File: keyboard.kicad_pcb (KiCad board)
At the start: 2 copper layers, 208.8 x 114.3 mm, 52 parts, among them J1 TRRS, SW00 Key, SW01 Key, SW02 Key, SW03 Key, SW04 Key, SW05 Key, SW10 Key, SW11 Key, SW12 Key, SW13 Key, SW14 Key, SW15 Key, SW16 Key, SW17 Key, SW18 Key, SW20 Key, SW21 Key, SW22 Key, SW23 Key, SW24 Key, SW25 Key, SW26 Key, SW27 Key, SW28 Key, SW30 Key, SW31 Key, SW32 Key, SW33 Key, SW34 Key, SW35 Key, SW36 Key, SW37 Key, SW38 Key, SW40 Key, SW41 Key, SW42 Key, SW43 Key, SW44 Key, SW45 Key, SW46 Key, SW47 Key, SW48 Key, U1 ProMicro

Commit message: rename files
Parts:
- H1: footprint myles-keyboard:RightPlate -> keyboard:RightPlate
- J1: footprint myles-keyboard:PJ-320A -> keyboard:PJ-320A
- JP1, JP2: footprint myles-keyboard:Jumper -> keyboard:Jumper
- JP3, JP4: footprint myles-keyboard:JumperSplit -> keyboard:JumperSplit
- R1, R2: footprint myles-keyboard:SDR18 -> keyboard:SDR18
- SW00, SW04, SW05, SW10, SW14, SW20, SW30: footprint myles-keyboard:KeyLeft -> keyboard:KeyLeft
- SW01, SW02, SW11, SW12, SW13, SW15, SW16, SW17, SW21, SW22, SW23, SW24, SW25, SW26, SW27, SW31, SW32, SW33, SW34, SW35, SW36, SW37, SW40, SW41, SW42, SW43, SW44, SW46, SW47: footprint myles-keyboard:Key -> keyboard:Key
- SW03, SW18, SW28, SW38, SW45, SW48: footprint myles-keyboard:KeyRight -> keyboard:KeyRight
- SW_RST1: footprint myles-keyboard:PTS636 -> keyboard:PTS636
- U1: footprint myles-keyboard:ProMicro -> keyboard:ProMicro

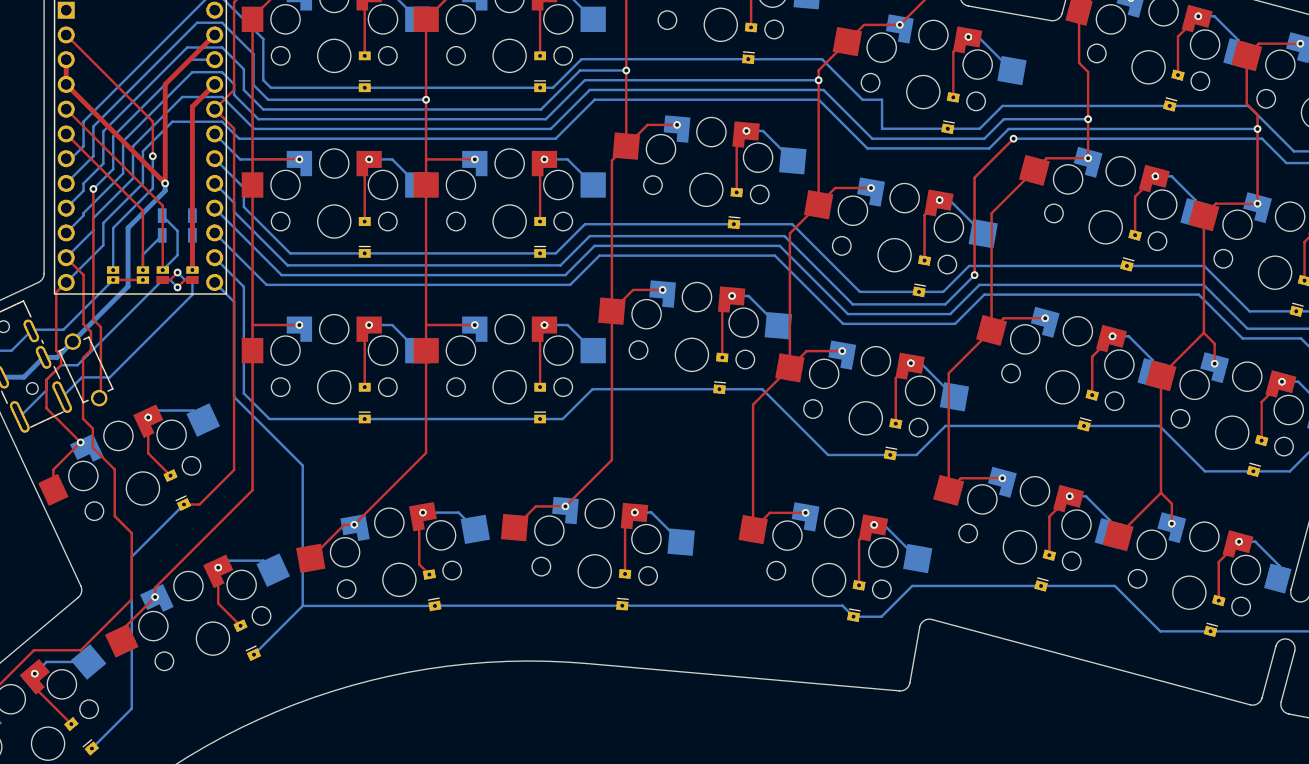
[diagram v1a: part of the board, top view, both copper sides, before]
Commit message: adjust plates and pcb; remove reset button
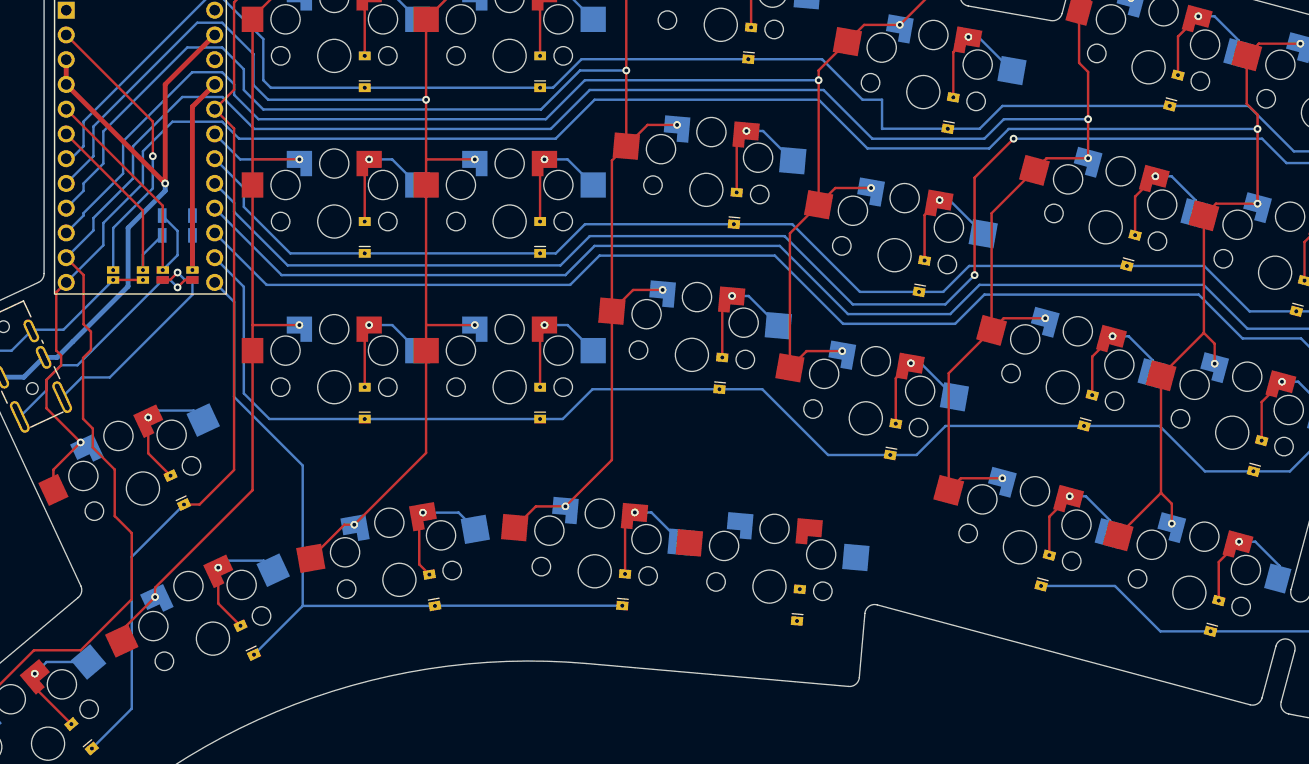
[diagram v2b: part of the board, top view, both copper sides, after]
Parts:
- removed SW_RST1: SW_Push, keyboard:PTS636
- moved SW43 6.16 mm to (124.4, 114.0), turned to -5 degrees
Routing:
- net row4: track 203.9 -> 159.1 mm
- net RESET: track 41.8 -> 0.00 mm, vias 1 -> 0
- net col3: track 201.4 -> 175.5 mm, vias 6 -> 5
- net Net-(SW43-Pad3): track 12.7 -> 0.00 mm, vias 1 -> 0
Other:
- outline, holes or cut-outs redrawn

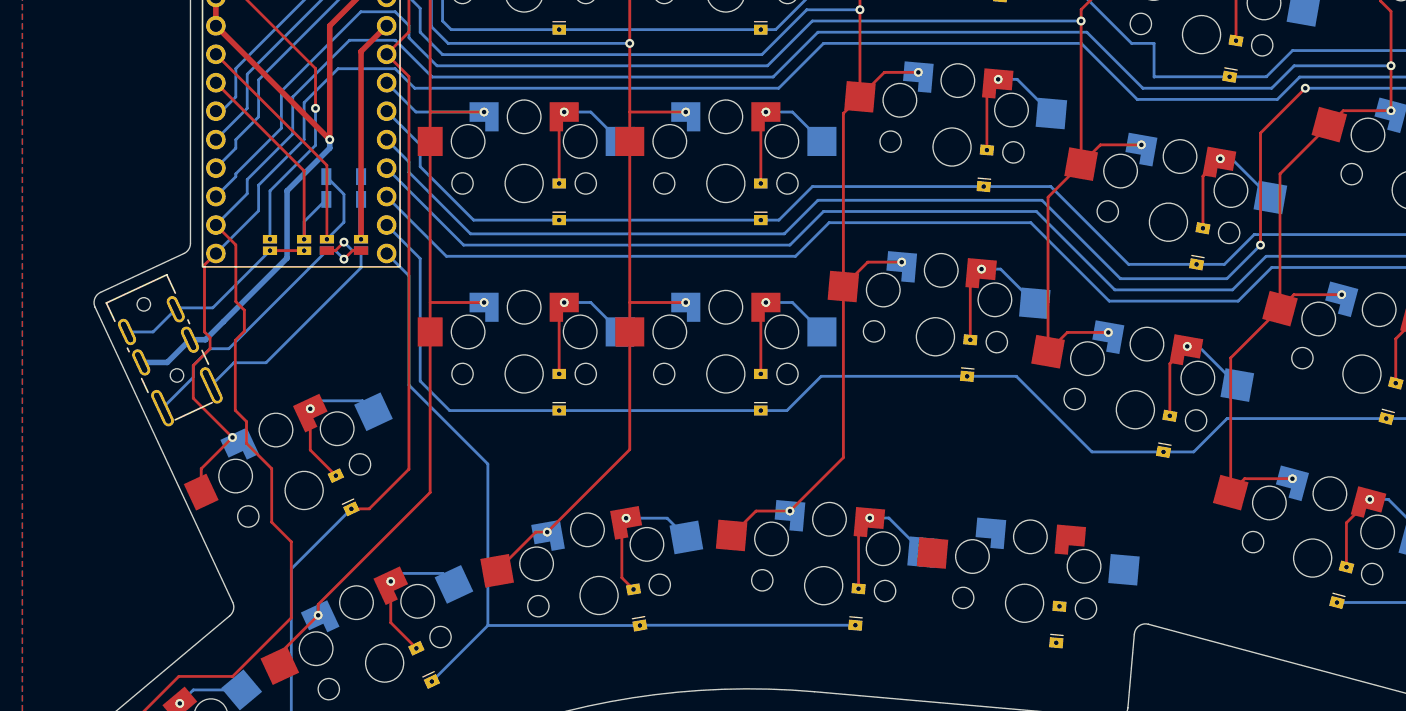
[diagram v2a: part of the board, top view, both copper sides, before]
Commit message: add symbol and footprint for new thin reset button
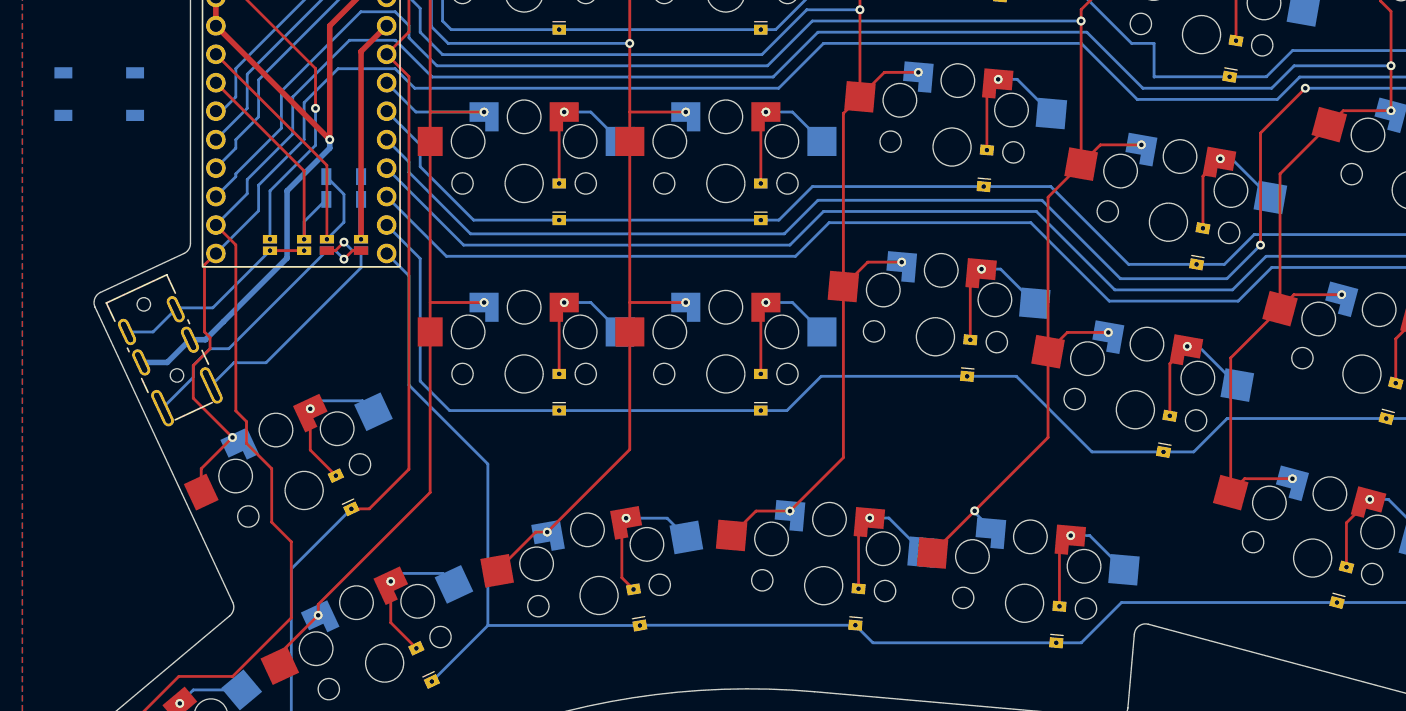
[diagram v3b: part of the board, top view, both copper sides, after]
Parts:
- added SW_RST1: PTS525, keyboard:PTS525, B.Cu at (41.9, 68.5)
- JP1, JP2: value JumperSplit -> Jumper
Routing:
- net row4: track 159.1 -> 204.3 mm
- net col3: track 175.5 -> 199.9 mm, vias 5 -> 6
- net Net-(SW43-Pad3): track 0.00 -> 12.7 mm, vias 0 -> 1
- net col4: track 263.7 -> 263.1 mm

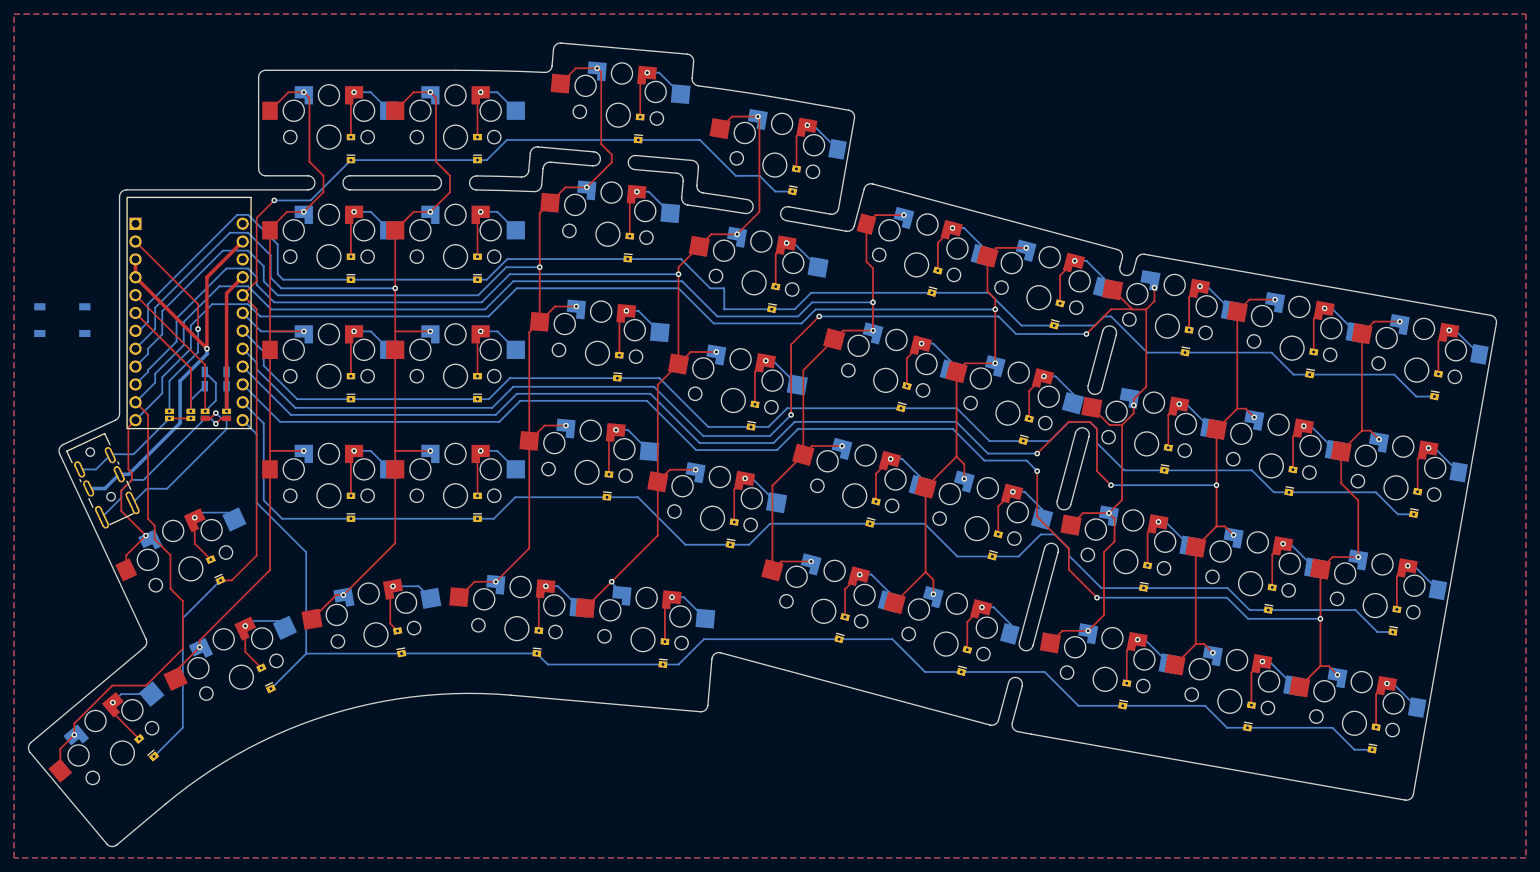
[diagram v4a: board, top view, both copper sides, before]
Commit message: reroute with new layout; use less vias in each switch
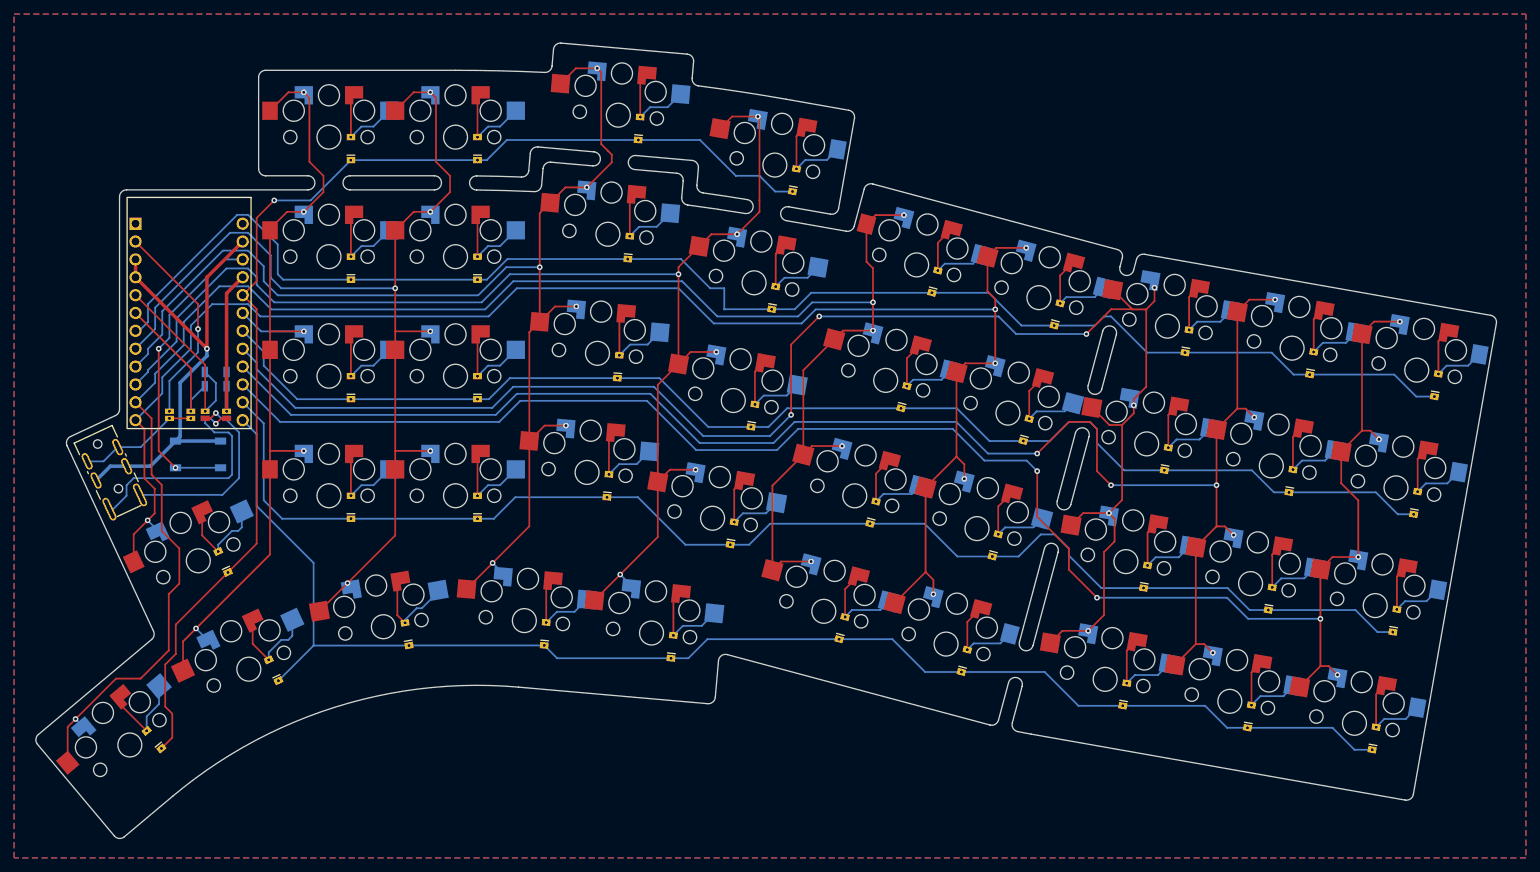
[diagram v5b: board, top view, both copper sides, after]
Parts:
- moved SW_RST1 27.2 mm to (61.2, 87.6), turned to 0 degrees
- moved SW42 1.56 mm to (107.6, 111.3)
- moved SW40 1.56 mm to (68.4, 118.2)
- moved SW04 1.56 mm to (51.5, 128.9)
- moved SW05 1.56 mm to (61.2, 102.8)
- moved J1 1.56 mm to (48.8, 90.2)
- moved SW41 1.56 mm to (87.5, 112.1)
- moved SW43 1.54 mm to (125.7, 113.0), turned to -6.171 degrees
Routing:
- net RESET: track 0.00 -> 43.4 mm, vias 0 -> 2
- net Net-(J1-Pad3): track 24.8 -> 34.8 mm
- net GND: track 63.3 -> 69.3 mm
- net Net-(J1-Pad4): track 22.9 -> 28.0 mm
- net row4: track 204.3 -> 202.2 mm
- net row0: track 169.0 -> 167.4 mm
- net col3: track 199.9 -> 198.3 mm
- net Net-(J1-Pad1): track 18.8 -> 17.3 mm
- net col1: track 153.0 -> 151.6 mm
- net Net-(SW40-Pad3): track 13.3 -> 14.6 mm, vias 1 -> 0
- net col4: track 263.1 -> 261.8 mm
- net Net-(SW38-Pad3): track 12.5 -> 13.8 mm, vias 1 -> 0
- net Net-(SW48-Pad3): track 12.5 -> 13.8 mm, vias 1 -> 0
- net Net-(SW03-Pad3): track 12.5 -> 13.8 mm, vias 1 -> 0
- net Net-(SW18-Pad3): track 12.5 -> 13.8 mm, vias 1 -> 0
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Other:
- board size 208.8 x 114.3 mm -> 207.7 x 113.1 mm

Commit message: remove two thumb keys
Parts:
- removed SW04: Key, keyboard:KeyLeft
- removed the SW43 at (125.7, 113.0)
- SW20, SW30: footprint keyboard:KeyLeft -> keyboard:Key
- SW41: renamed from SW40; footprint keyboard:Key -> keyboard:KeyLeft
- SW43: renamed from SW42; footprint keyboard:Key -> keyboard:KeyRight
- renumbered SW05 to SW40, SW41 to SW42
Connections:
- SW40 pad 1: col5 -> col0
- SW40 pad 2: col5 -> col0
- SW40 pad 6: row0 -> row4
- SW41 pad 1: col0 -> col1
- SW41 pad 2: col0 -> col1
- SW42 pad 1: col1 -> col2
- SW42 pad 2: col1 -> col2
- SW43 pad 1: col2 -> col3
- SW43 pad 2: col2 -> col3
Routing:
- net row0: track 167.4 -> 95.6 mm
- net col4: track 261.8 -> 196.2 mm, vias 6 -> 5
- net col5: track 233.6 -> 209.1 mm, vias 6 -> 5
- net col1: track 151.6 -> 171.9 mm
- net col2: track 178.0 -> 195.5 mm
- net col3: track 198.3 -> 212.3 mm
- net Net-(SW43-Pad3) (its old number): track 13.9 -> 0.00 mm
- net Net-(SW04-Pad3): track 13.8 -> 0.00 mm
- net row4: track 202.2 -> 209.2 mm
- net col0: track 120.7 -> 125.7 mm
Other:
- board size 207.7 x 113.1 mm -> 203.4 x 107.7 mm
